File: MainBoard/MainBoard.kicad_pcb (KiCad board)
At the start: 2 copper layers, 50 x 50 mm, 12 parts, among them P1 CONN_01X07, P2 CONN_01X04, P3 CONN_01X04, P4 CONN_01X07, P5 ON/OFF, P6 BATTERY, U1 4056_CARG

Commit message: Correction tracks
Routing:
- net Net-(D1-Pad2): track 47.1 -> 55.6 mm
- net +BATT: track 133.0 -> 136.4 mm
- net /MOSI: track 22.3 -> 25.5 mm
- net /NSS: track 23.8 -> 26.8 mm
- net /A0: track 34.5 -> 36.9 mm
- net GND: track 89.8 -> 92.1 mm
- net /A1: track 35.9 -> 36.9 mm
- net /S_RX: track 15.2 -> 16.0 mm
- net /S_TX: track 16.0 -> 16.7 mm
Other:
- net class Default: trace_width 0.25 -> 0.3

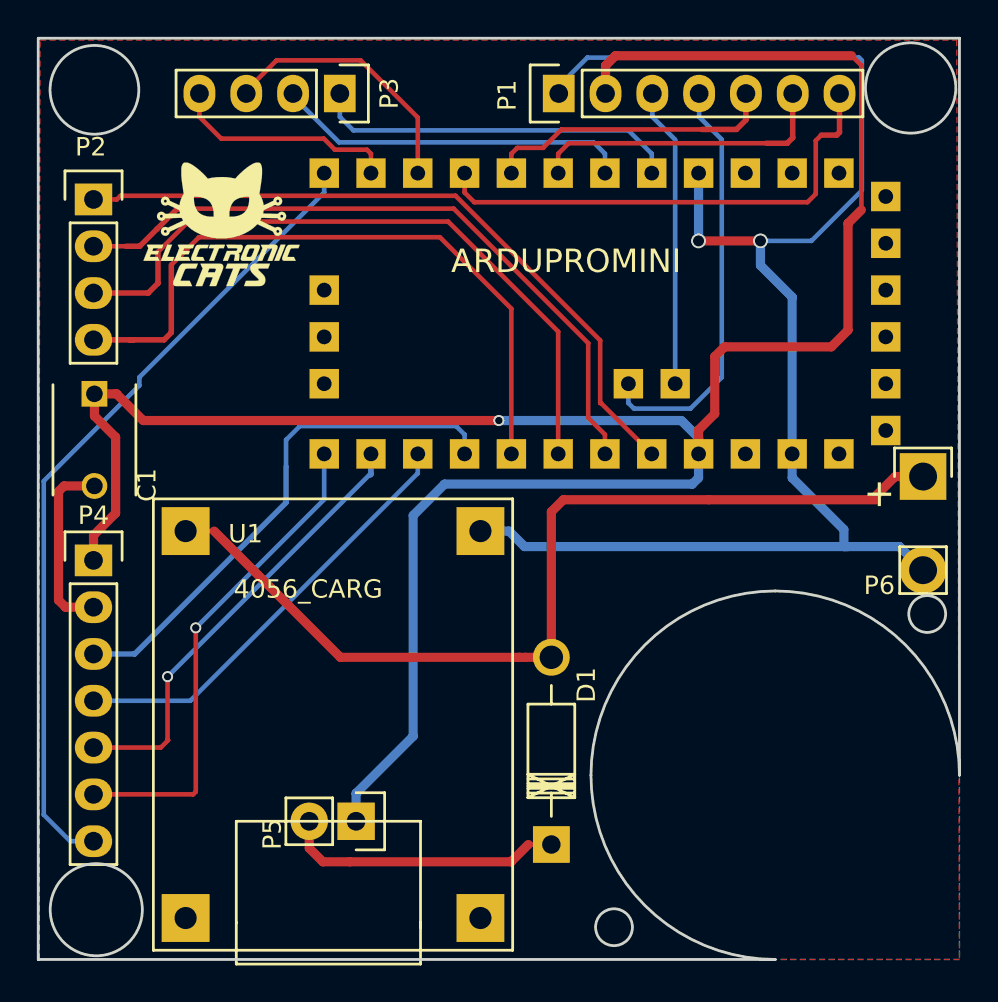
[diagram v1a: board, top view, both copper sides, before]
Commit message: Add larger holes
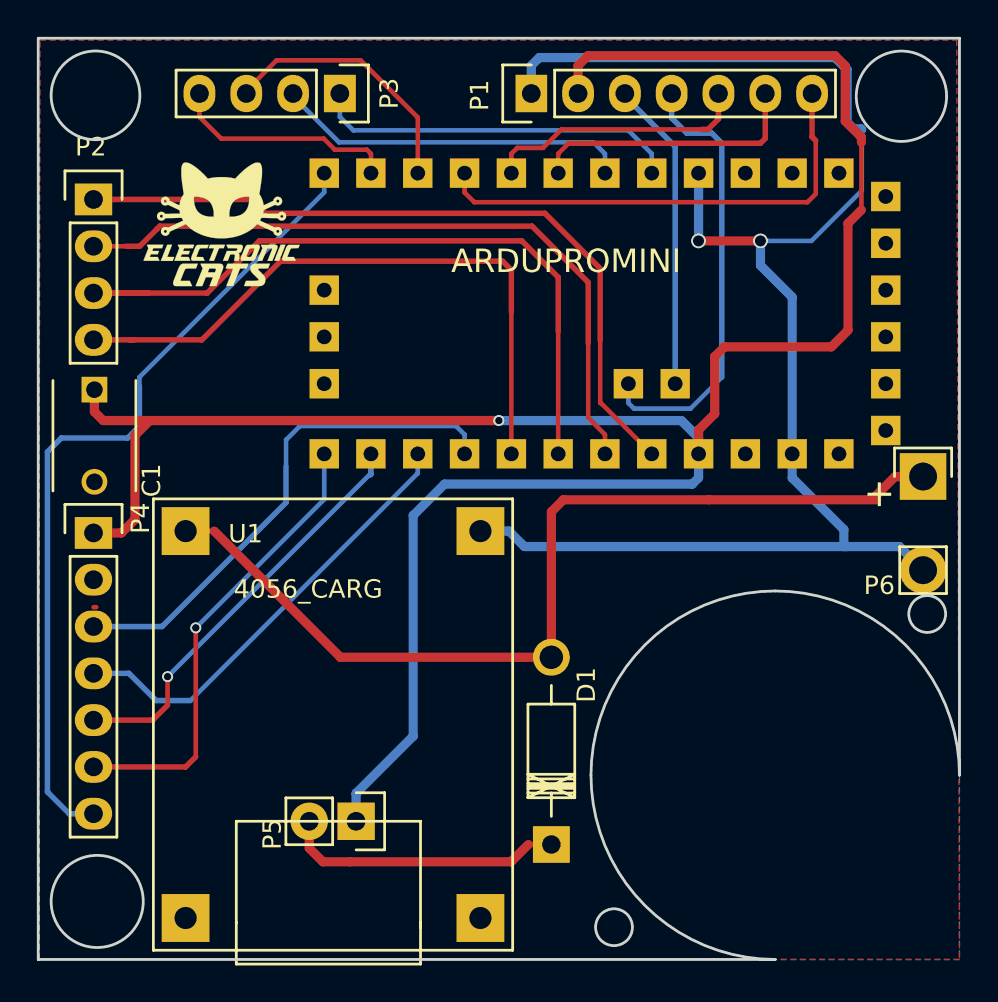
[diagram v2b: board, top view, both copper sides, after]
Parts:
- moved P1 1.49 mm to (111.3, 56.9)
- moved P4 1.49 mm to (87.5, 80.8)
- moved C1 0.23 mm to (87.6, 73.0)
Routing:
- net GND: track 92.1 -> 83.5 mm
- net /A1: track 36.9 -> 39.8 mm
- net /A3: track 38.5 -> 40.7 mm
- net /A0: track 36.9 -> 35.0 mm
- net /MOSI: track 25.5 -> 23.8 mm
- net /NSS: track 26.8 -> 25.1 mm
- net /S_TX: track 16.7 -> 15.1 mm
- net /S_RX: track 16.0 -> 14.5 mm
- net /SDA: track 22.9 -> 24.3 mm
- net /A2: track 37.1 -> 38.3 mm
- net /DHT/D6: track 27.0 -> 26.0 mm
- net /MISO: track 23.8 -> 24.4 mm
- net /SCK: track 28.5 -> 27.9 mm
- net /SCL: track 16.3 -> 16.9 mm
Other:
- outline, holes or cut-outs redrawn

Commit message: Remove pines FTDI Arduino mini
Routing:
- net +BATT: track 136.4 -> 137.4 mm
